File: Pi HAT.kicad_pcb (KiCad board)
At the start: 2 copper layers, 65 x 41.5 mm, 69 parts, among them IC1 AD7730, J1 Screw_Terminal_01x04, J11 Conn_01x02_Male, J4 Barrel_Jack, J5 Screw_Terminal_01x03, J6 Screw_Terminal_01x03, J7 GPIO_CONNECTOR, J9 Conn_01x03_Male, K1 SANYOU_SRD_Form_C, K2 SANYOU_SRD_Form_C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

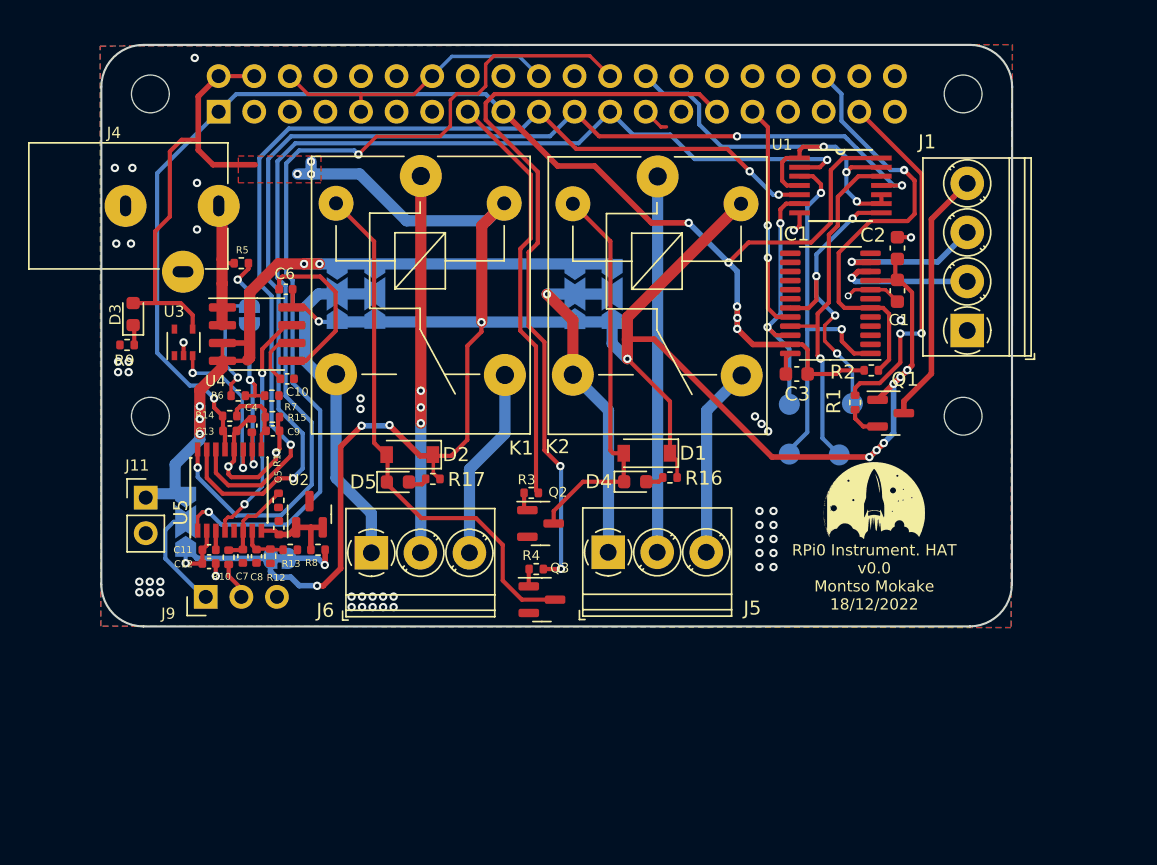
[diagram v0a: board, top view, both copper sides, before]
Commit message: Added footprints for HX711 circuit on PCB and modified pin assignment
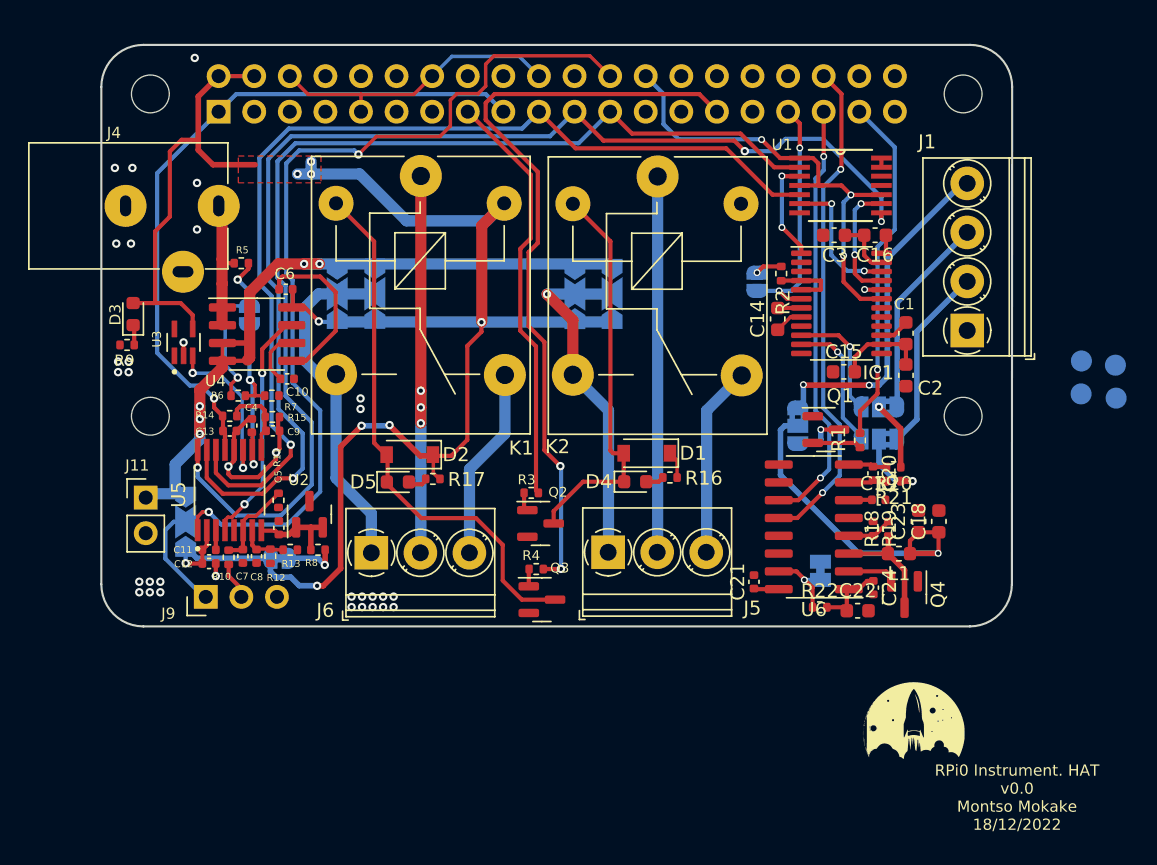
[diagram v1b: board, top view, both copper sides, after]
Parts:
- added C14: 100n, Capacitor_SMD:C_0603_1608Metric, F.Cu at (165.8, 110.6)
- added C15: 100nF, Capacitor_SMD:C_0603_1608Metric, F.Cu at (170.5, 114.4)
- added C16: 100n, Capacitor_SMD:C_0603_1608Metric, F.Cu at (172.8, 104.7)
- added C18: 10uF, Capacitor_SMD:C_0603_1608Metric, F.Cu at (177.3, 125.1)
- added C19: 100nF, Capacitor_SMD:C_0402_1005Metric, F.Cu at (173.0, 123.5)
- added C20: 100nF, Capacitor_SMD:C_0402_1005Metric, F.Cu at (172.6, 121.6)
- added C21: 100nF, Capacitor_SMD:C_0402_1005Metric, F.Cu at (164.1, 129.4)
- added C22: 10uF, Capacitor_SMD:C_0603_1608Metric, F.Cu at (171.5, 131.4)
- added C23: 10uF, Capacitor_SMD:C_0603_1608Metric, F.Cu at (175.8, 125.1)
- added C24: 100nF, Capacitor_SMD:C_0402_1005Metric, F.Cu at (172.6, 129.8)
- added JP10: RATE, Jumper:SolderJumper-2_P1.3mm_Bridged_Pad1.0x1.5mm, B.Cu at (168.8, 128.6)
- added JP11: S-, Jumper:SolderJumper-3_P1.3mm_Bridged2Bar12_RoundedPad1.0x1.5mm, B.Cu at (173.0, 119.2)
- added JP12: EXCITATION, Jumper:SolderJumper-3_P1.3mm_Bridged2Bar12_RoundedPad1.0x1.5mm, B.Cu at (167.2, 118.2)
- added JP8: Jumper_NO_Small, Jumper:SolderJumper-2_P1.3mm_Open_RoundedPad1.0x1.5mm, B.Cu at (164.3, 108.0)
- added JP9: S+, Jumper:SolderJumper-3_P1.3mm_Bridged2Bar12_RoundedPad1.0x1.5mm, B.Cu at (173.0, 116.9)
- added L1: 3.3uH, Inductor_SMD:L_0603_1608Metric, F.Cu at (174.4, 127.4)
- added Q4: S8550, Package_TO_SOT_SMD:SOT-23, F.Cu at (174.8, 130.3)
- added R18: 33k, Resistor_SMD:R_0402_1005Metric, F.Cu at (173.7, 125.6)
- added R19: 12k, Resistor_SMD:R_0402_1005Metric, F.Cu at (172.6, 125.6)
- added R20: 100R, Resistor_SMD:R_0402_1005Metric, F.Cu at (174.1, 121.2)
- added R21: 100R, Resistor_SMD:R_0402_1005Metric, F.Cu at (174.1, 122.2)
- added R22: 10k, Resistor_SMD:R_0402_1005Metric, F.Cu at (168.8, 131.2)
- added U6: HX711, Package_SO:SOP-16_3.9x9.9mm_P1.27mm, F.Cu at (168.4, 125.5)
- C2: value 10uF -> 100n
- U3: footprint Package_TO_SOT_SMD:SOT-353_SC-70-5 -> TMP235A2DCKR:SOT65P210X110-5N
- U5: footprint Package_SO:SSOP-16_4.4x5.2mm_P0.65mm -> ADC108S022CIMTX_NOPB:SOP65P640X120-16N
- moved TP5 21.9 mm to (187.5, 113.6)
- moved TP7 20.8 mm to (187.4, 116.0)
- moved TP8 20.2 mm to (189.9, 116.3)
- moved TP6 19.0 mm to (189.9, 113.9)
- moved G*** 16.0 mm to (175.3, 139.7)
- moved C3 10.3 mm to (169.8, 104.7)
- moved R2 9.43 mm to (166.1, 107.4), turned to -90 degrees
- moved C2 9.10 mm to (174.9, 114.7), turned to 90 degrees
- moved Q1 4.77 mm to (169.2, 118.5)
- moved C1 3.10 mm to (174.9, 111.7), turned to -90 degrees
- moved R1 2.73 mm to (171.7, 119.3)
- moved IC1 0.79 mm to (170.3, 109.5), turned to 0 degrees
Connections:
- C13 pad 1: +3V3 -> +3.3V
- C3 pad 2: +3V3 -> +3.3V
- IC1 pad 10: /Instumentaional Amp/AIN1+ -> /AIN1+
- IC1 pad 11: /Instumentaional Amp/AIN1- -> /AIN1-
- IC1 pad 12: /Instumentaional Amp/AIN2+ -> unconnected-(IC1-AIN2+/D1-Pad12)
- IC1 pad 13: /Instumentaional Amp/AIN2- -> unconnected-(IC1-AIN2-/D0-Pad13)
- IC1 pad 14: unconnected-(IC1-Pad14) -> +5V
- IC1 pad 15: unconnected-(IC1-Pad15) -> GND
- IC1 pad 18: unconnected-(IC1-Pad18) -> +3.3V
- IC1 pad 19: /Instumentaional Amp/SPI_!CS_BUFF -> /GPIO7_SPI_CE1_N
- IC1 pad 23: +3V3 -> +3.3V
- IC1 pad 4: unconnected-(IC1-Pad4) -> +3.3V
- IC1 pad 5: unconnected-(IC1-Pad5) -> +3.3V
- IC1 pad 6: /GPIO16 -> /GPIO13
- IC1 pad 7: unconnected-(IC1-Pad7) -> Net-(IC1-VBIAS)
- J1 pad 1: /LOAD_CELL_PWR -> /LOAD_CELL_EXC
- J1 pad 2: /Instumentaional Amp/AIN1- -> /S+
- J1 pad 3: /Instumentaional Amp/AIN1+ -> /S-
- J7 pad 1: +3V3 -> +3.3V
- J7 pad 17: +3V3 -> +3.3V
- Q2 pad 1: Net-(Q2-Pad1) -> GND
- Q2 pad 2: GND -> Net-(Q2-B)
- Q3 pad 1: Net-(Q3-Pad1) -> GND
- Q3 pad 2: GND -> Net-(Q3-B)
- R14 pad 1: +3V3 -> +3.3V
- R2 pad 1: /GPIO16 -> Net-(JP8-A)
- R2 pad 2: +3V3 -> +3.3V
- R3 pad 1: Net-(Q2-Pad1) -> Net-(Q2-B)
- R4 pad 1: Net-(Q3-Pad1) -> Net-(Q3-B)
- TP6 pad 1: /Instumentaional Amp/SPI_!CS_BUFF -> /GPIO7_SPI_CE1_N
- U1 pad 11: /GPIO9_SPI_MISO -> unconnected-(U1-4Y-Pad11)
- U1 pad 12: /Instumentaional Amp/SPI_MISO_BUFF -> unconnected-(U1-4A-Pad12)
- U1 pad 13: /GPIO7_SPI_CE1_N -> +3.3V
- U1 pad 14: +3V3 -> +3.3V
- U1 pad 8: /Instumentaional Amp/SPI_!CS_BUFF -> /GPIO9_SPI_MISO
- U1 pad 9: /GPIO7_SPI_CE1_N -> /Instumentaional Amp/SPI_MISO_BUFF
- U5 pad 13: +3V3 -> +3.3V
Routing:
- net +3V3: track 104.6 -> 0.00 mm, vias 6 -> 0
- net +3.3V: track 0.00 -> 61.3 mm, vias 0 -> 1
- net +5V: track 202.5 -> 145.3 mm, vias 16 -> 9
- net /GPIO19_SPI_MISO: track 0.00 -> 30.7 mm, vias 0 -> 2
- net /EXC+: track 0.00 -> 24.9 mm, vias 0 -> 1
- net /LOAD_CELL_EXC: track 0.00 -> 24.3 mm, vias 0 -> 2
- net /Instumentaional Amp/SPI_!CS_BUFF: track 22.0 -> 0.00 mm, vias 4 -> 0
- net /Instumentaional Amp/SPI_SCL_BUFF: track 27.7 -> 7.37 mm
- net /GPIO13: track 0.00 -> 17.4 mm, vias 0 -> 2
- net /Instumentaional Amp/SPI_MISO_BUFF: track 25.3 -> 8.74 mm, vias 1 -> 2
- net /GPIO6: track 16.3 -> 1.22 mm, vias 2 -> 1
- net /LOAD_CELL_PWR: track 18.3 -> 3.40 mm, vias 0 -> 1
- net /S+: track 0.00 -> 14.5 mm
- net /S-: track 0.00 -> 13.3 mm
- net /Instumentaional Amp/AIN1-: track 10.5 -> 0.00 mm, vias 1 -> 0
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- removed copper zone on B.Cu, net GND
- removed copper zone on F.Cu, net GND

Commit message: Fixed clearance violations and via sizing violations on pcb. Omitted 'mask aperture bridges' errors for jumpers.
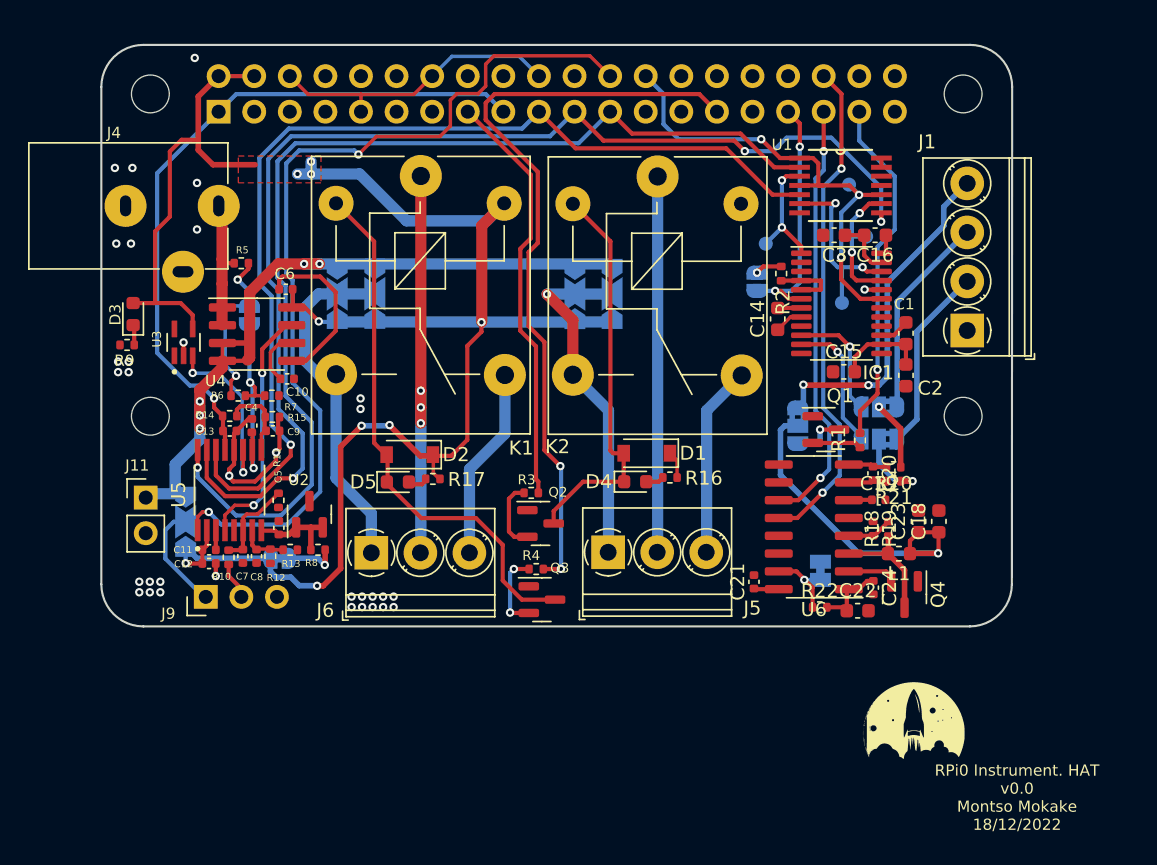
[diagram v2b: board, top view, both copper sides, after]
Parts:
- TP5, TP6, TP7, TP8: footprint TestPoint:TestPoint_Pad_D1.5mm -> TestPoint:TestPoint_Pad_D1.0mm
- moved TP5 24.0 mm to (164.9, 105.3)
- moved TP6 23.0 mm to (170.9, 101.0)
- moved TP8 21.2 mm to (172.1, 104.7)
- moved TP7 18.3 mm to (170.4, 109.5)
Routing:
- net Net-(Q3-B): track 0.00 -> 5.66 mm, vias 0 -> 2
- net Net-(Q2-B): track 0.00 -> 5.07 mm
- net /Instumentaional Amp/SPI_MOSI_BUFF: track 10.0 -> 13.3 mm
- net GND: track 56.8 -> 54.6 mm
- net /Instumentaional Amp/SPI_SCL_BUFF: track 7.37 -> 8.81 mm
- net /GPIO7_SPI_CE1_N: track 33.8 -> 35.2 mm
- net /Instumentaional Amp/SPI_MISO_BUFF: track 8.74 -> 9.81 mm
- net /Power Monitor/ADC7: track 11.9 -> 12.5 mm
- net /GPIO9_SPI_MISO: track 83.9 -> 84.6 mm
- net /Power Monitor/ADC0: track 17.1 -> 17.7 mm

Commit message: Added ground pour and fixed connections
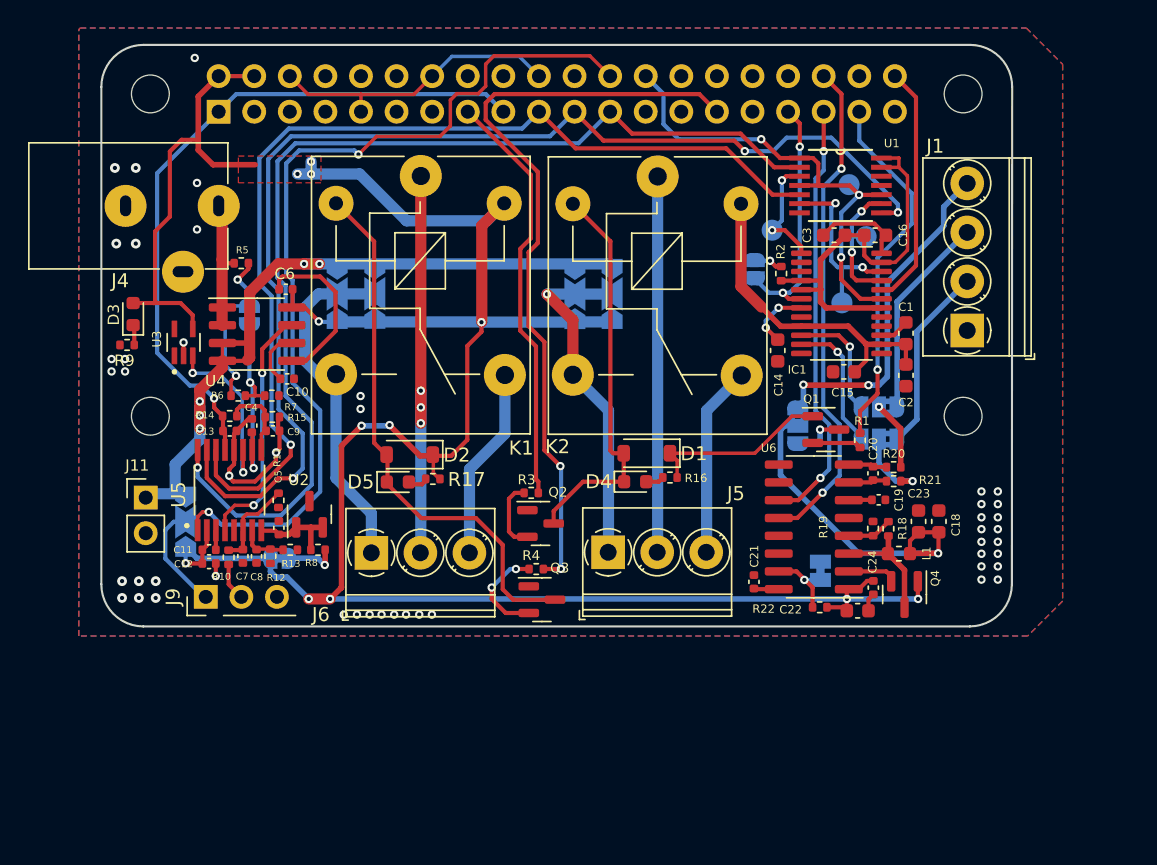
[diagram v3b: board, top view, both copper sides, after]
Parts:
- removed G***: LOGO, LOGO
- TP5, TP6, TP7, TP8: footprint TestPoint:TestPoint_Pad_D1.0mm -> TestPoint:TestPoint_Pad_D1.5mm
- moved C14 2.25 mm to (165.8, 112.9)
- moved TP5 1.07 mm to (165.4, 104.3)
- moved JP8 0.92 mm to (164.1, 107.1)
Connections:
- net /Relays/DC_SIDE1 renamed /Relays/NO1
- net /Relays/DC_SIDE2 renamed /Relays/NO2
- IC1 pad 20: /GPIO6 -> /GPIO21_SPI_SCLK
- J1 pad 1: /LOAD_CELL_EXC -> GND
- J1 pad 2: /S+ -> /S-
- J1 pad 3: /S- -> /S+
- J1 pad 4: GND -> /LOAD_CELL_EXC
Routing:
- net +5V: track 145.3 -> 219.6 mm, vias 9 -> 12
- net +3.3V: track 61.3 -> 81.5 mm
- net /GPIO21_SPI_SCLK: track 0.00 -> 17.3 mm
- net GND: track 54.6 -> 58.8 mm, vias 33 -> 47
- net Net-(IC1-VBIAS): track 1.80 -> 4.64 mm, vias 0 -> 2
- net Net-(Q3-B): track 5.66 -> 7.09 mm
- net /GPIO6: track 1.22 -> 0.00 mm, vias 1 -> 0
- net /GPIO26: track 25.0 -> 26.0 mm
- net /Instumentaional Amp/SPI_SCL_BUFF: track 8.81 -> 8.27 mm
- added copper zone on B.Cu, net GND
- added copper zone on F.Cu, net GND

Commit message: Updated +3V3 tracks on pcb and buffer schematic
-Added decoupling cap for buffer
-Tied unused buffer input 4 to gnd
-Did all +3V3 connections
-Fixed +5V tracks
-gnd stitching
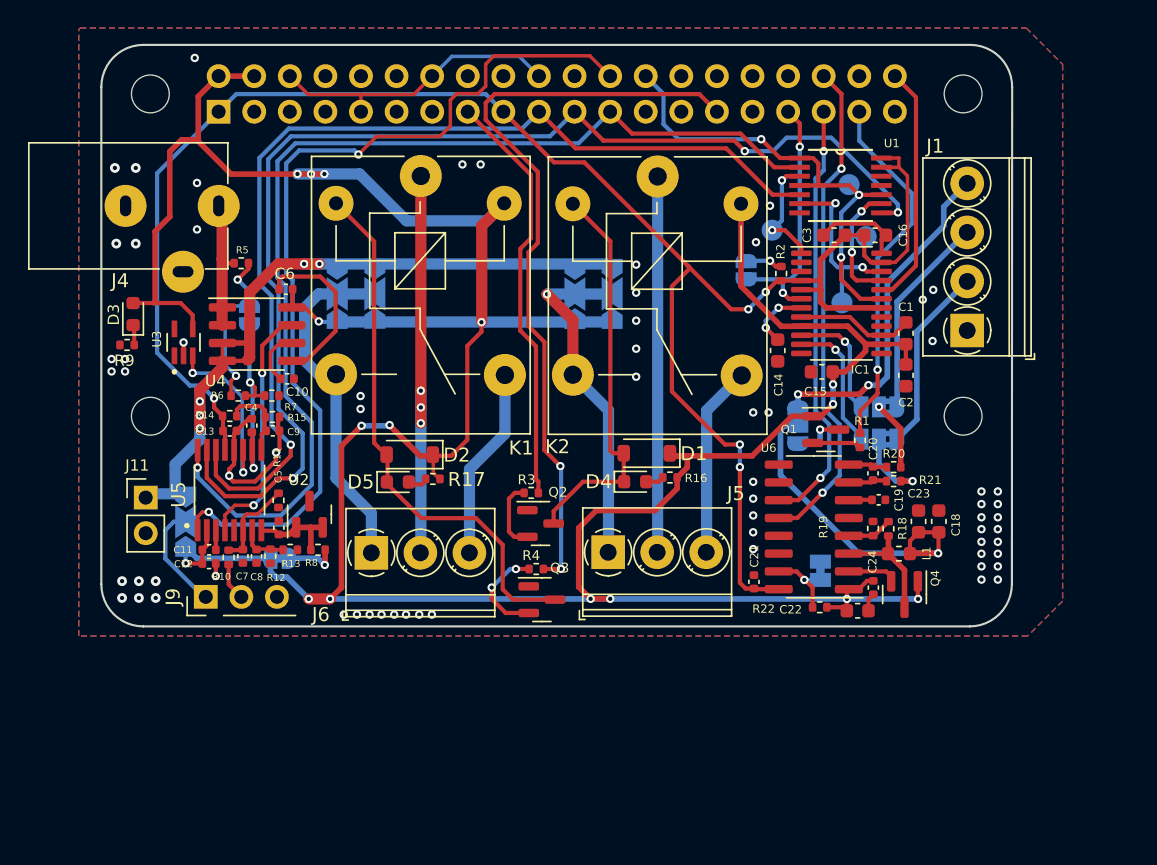
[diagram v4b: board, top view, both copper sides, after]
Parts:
- moved C15 1.58 mm to (168.9, 114.4)
- moved JP8 0.59 mm to (163.6, 107.2)
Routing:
- net +3.3V: track 81.5 -> 135.1 mm, vias 1 -> 5
- net +5V: track 219.6 -> 246.0 mm, vias 12 -> 16
- net GND: track 58.8 -> 65.1 mm, vias 47 -> 66
- net Net-(JP8-A): track 2.10 -> 2.68 mm
- removed copper zone on F.Cu, net +5V

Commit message: Updated power circuit. Fixed U1 footprint.
-Dropped ADC1 and ADC3 connections
-Dropped IN1 branch
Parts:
- removed C8: 1n, Capacitor_SMD:C_0402_1005Metric
- removed R12, R13: 220R, Resistor_SMD:R_0402_1005Metric
- added C17: 100n, Capacitor_SMD:C_0603_1608Metric, F.Cu at (174.9, 105.8)
- JP10: footprint Jumper:SolderJumper-2_P1.3mm_Bridged_Pad1.0x1.5mm -> Jumper:SolderJumper-2_P1.3mm_Open_RoundedPad1.0x1.5mm
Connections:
- U1 pad 12: unconnected-(U1-4A-Pad12) -> GND
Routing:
- net /Power Monitor/ADC3: track 3.40 -> 0.00 mm
- net GND: track 65.1 -> 66.7 mm
- net +3.3V: track 135.1 -> 136.2 mm
- net /GPIO21_SPI_SCLK: track 17.3 -> 18.4 mm
